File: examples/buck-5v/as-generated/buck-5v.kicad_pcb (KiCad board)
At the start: 2 copper layers, 126 x 56 mm, 11 parts, among them J1 12V IN, J2 5V OUT, U1 LM2596S-5

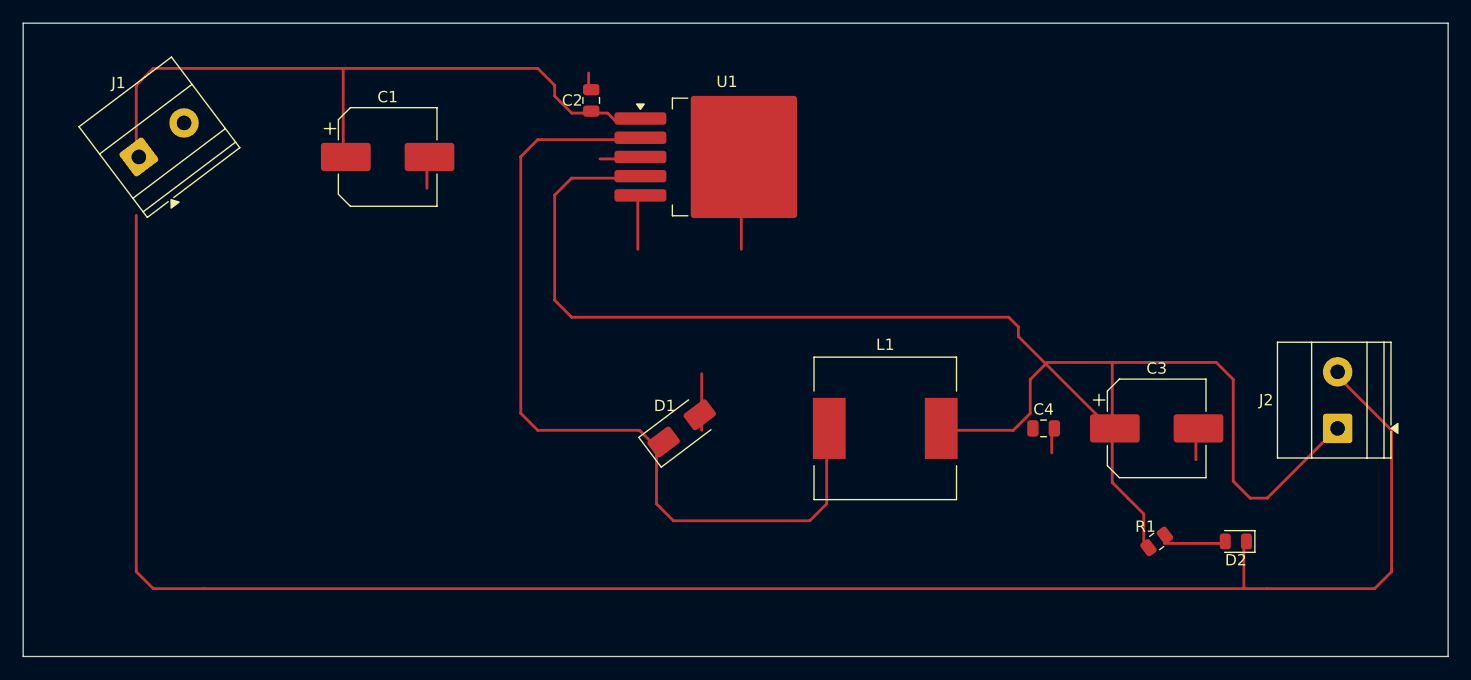
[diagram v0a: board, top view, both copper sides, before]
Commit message: Measure the copper that goes out and comes back, and the text drawn on text
The reviewer sent screenshots with circles on them. Two kinds: strings
printed through each other on the schematics, and copper that leaves a
pad, travels three sides of a rectangle and arrives four millimetres
away. Neither had a rule that could see it - `text_over_wire` measured
text against nets and nothing measured text against text, and
`route.detour` weighs a whole net, which averages one bad connection
away under any ratio worth setting.

New rule `route.wander`: one continuous run of copper - pad or junction
at each end - against the shortest way between those two ends that
clears the packages in between. The baseline walks the perimeter of
whatever the straight line crosses, so an opamp's feedback wrap is
measured against going round the package rather than through it. On
KiCad's 18 demo boards it fires once at the shipped 2.0x.

`readability.text_over_text` and `_over_wire` are regraded info: they
fire on 14 and 10 of those 18 human sheets. That is the estimate
talking, not the drawing. `ai-generated` still promotes both to errors,
so every generated design has to have none - and the five examples do.

What the two rules then made us fix:

* a net label's anchor cannot move, but its reading direction can. Each
  name is now offered the four quarters of its anchor and takes the
  first that prints over nothing. Power symbol names and PWR_FLAG names
  get the same treatment - four grounds on one row printed GNGNGNGND.
  Schematic text overlaps: buck 1, motor 2, carrier 1, fpga 7, all to 0.
* a plane crossing was priced at forty times front copper per
  millimetre, which is a prohibition, not a price: one millimetre of
  crossing bought a forty millimetre tour and the boards had grown
  them. Thirty is where neither `route.wander` nor `route.return_path`
  fires. Buck, motor and carrier now have no wander findings.
* `write_variant` resolves the routes a second time, so the
  straight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
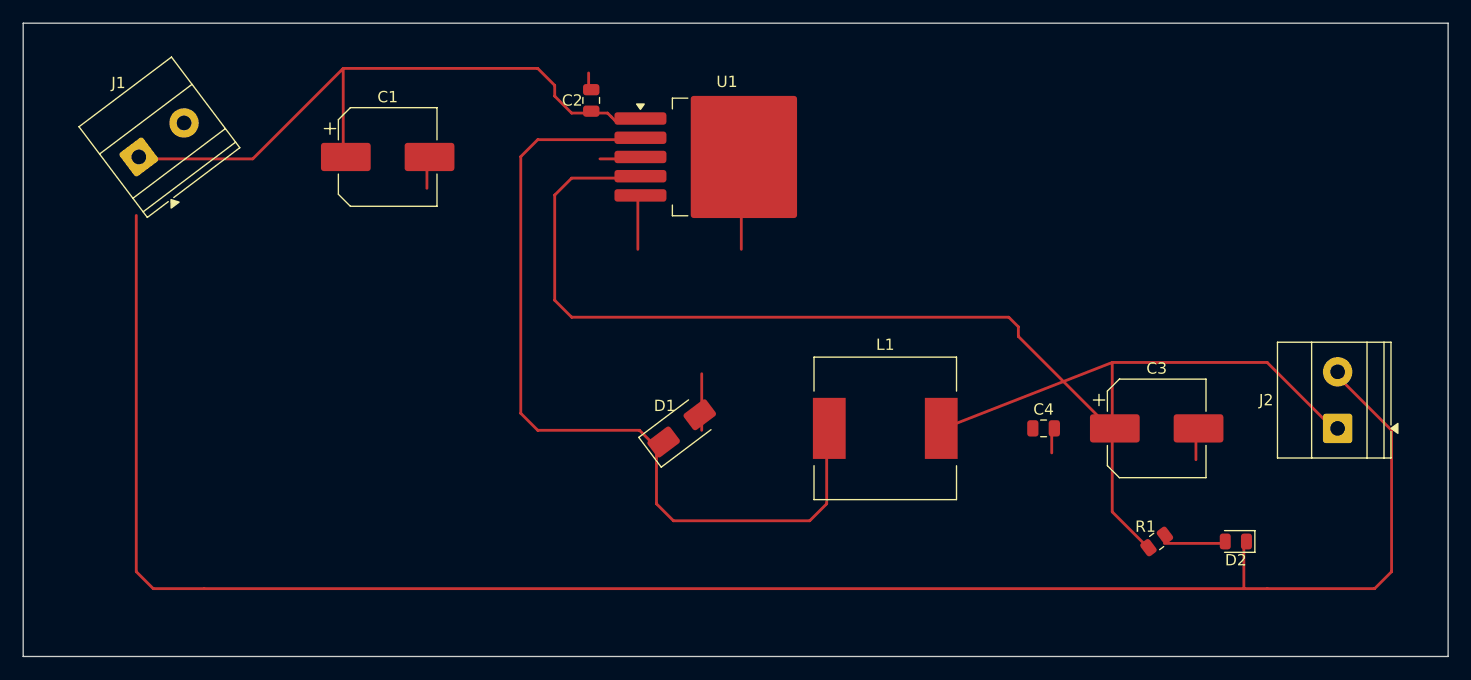
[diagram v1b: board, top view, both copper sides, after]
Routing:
- net /+5V: track 141.0 -> 127.7 mm
- net /+12V: track 61.9 -> 58.1 mm
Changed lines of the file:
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@@
 	(gr_line (start 226.0 116.0) (end 100.0 116.0) (stroke (width 0.1) (type default)) (layer "Edge.Cuts"))
 	(gr_line (start 100.0 116.0) (end 100.0 60.0) (stroke (width 0.1) (type default)) (layer "Edge.Cuts"))
-	(segment (start 110.0 72.0) (end 110.0 65.5) (width 0.25) (layer "F.Cu") (net 2))
-	(segment (start 110.0 65.5) (end 111.5 64.0) (width 0.25) (layer "F.Cu") (net 2))
-	(segment (start 111.5 64.0) (end 128.3 64.0) (width 0.25) (layer "F.Cu") (net 2))
+	(segment (start 110.0 72.0) (end 120.3 72.0) (width 0.25) (layer "F.Cu") (net 2))
+	(segment (start 120.3 72.0) (end 128.3 64.0) (width 0.25) (layer "F.Cu") (net 2))
 	(segment (start 128.3 64.0) (end 128.3 72.0) (width 0.25) (layer "F.Cu") (net 2))
 	(segment (start 128.3 64.0) (end 145.5 64.0) (width 0.25) (layer "F.Cu") (net 2))
@@
 	(segment (start 188.0 86.85) (end 188.0 87.7) (width 0.25) (layer "F.Cu") (net 3))
 	(segment (start 188.0 87.7) (end 196.3 96.0) (width 0.25) (layer "F.Cu") (net 3))
-	(segment (start 180.95 96.0) (end 187.55 96.0) (width 0.25) (layer "F.Cu") (net 3))
-	(segment (start 187.55 96.0) (end 189.05 94.5) (width 0.25) (layer "F.Cu") (net 3))
-	(segment (start 189.05 94.5) (end 189.05 91.5) (width 0.25) (layer "F.Cu") (net 3))
-	(segment (start 189.05 91.5) (end 190.55 90.0) (width 0.25) (layer "F.Cu") (net 3))
-	(segment (start 190.55 90.0) (end 196.3 90.0) (width 0.25) (layer "F.Cu") (net 3))
+	(segment (start 180.95 96.0) (end 196.3 90.0) (width 0.25) (layer "F.Cu") (net 3))
 	(segment (start 196.3 90.0) (end 196.3 96.0) (width 0.25) (layer "F.Cu") (net 3))
-	(segment (start 196.3 90.0) (end 205.5 90.0) (width 0.25) (layer "F.Cu") (net 3))
-	(segment (start 205.5 90.0) (end 207.0 91.5) (width 0.25) (layer "F.Cu") (net 3))
-	(segment (start 207.0 91.5) (end 207.0 100.5) (width 0.25) (layer "F.Cu") (net 3))
-	(segment (start 207.0 100.5) (end 208.5 102.0) (width 0.25) (layer "F.Cu") (net 3))
-	(segment (start 208.5 102.0) (end 210.0 102.0) (width 0.25) (layer "F.Cu") (net 3))
-	(segment (start 210.0 102.0) (end 216.0 96.0) (width 0.25) (layer "F.Cu") (net 3))
-	(segment (start 196.3 96.0) (end 196.3 100.606) (width 0.25) (layer "F.Cu") (net 3))
-	(segment (start 196.3 100.606) (end 197.694 102.0) (width 0.25) (layer "F.Cu") (net 3))
-	(segment (start 197.694 102.0) (end 199.088 103.394) (width 0.25) (layer "F.Cu") (net 3))
-	(segment (start 199.088 103.394) (end 199.0875 106.0) (width 0.25) (layer "F.Cu") (net 3))
+	(segment (start 196.3 90.0) (end 210.0 90.0) (width 0.25) (layer "F.Cu") (net 3))
+	(segment (start 210.0 90.0) (end 216.0 96.0) (width 0.25) (layer "F.Cu") (net 3))
+	(segment (start 196.3 96.0) (end 196.3 103.2125) (width 0.25) (layer "F.Cu") (net 3))
+	(segment (start 196.3 103.2125) (end 199.0875 106.0) (width 0.25) (layer "F.Cu") (net 3))
 	(segment (start 200.9125 106.0) (end 206.0625 106.0) (width 0.25) (layer "F.Cu") (net 4))
 	(segment (start 110.0 77.0) (end 110.0 108.5) (width 0.25) (layer "F.Cu") (net 1))

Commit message: Stop hiding the hairpins behind the pads they are drawn on
The reviewer said the 135 degree bends and the odd-angle runs were still
there. They were. `route.acute_angle` skipped any corner within a pad's
*radius*, and a 0805's radius is 0.47 mm, which covers the five or six
ordinary corners a chamfered pad entry leaves inside it. Eleven of the
thirteen hairpins on these five boards sat in that shadow, because a pad
is exactly where a route that has to double back does it.

The exemption is the pad's connection point now, not a disc around it.
Two branches leaving one pad stay exempt - the pad's own copper fills the
wedge, so it is not an acid trap - but nought degrees never is: that is
one run drawn twice, and no pad excuses it.

Then the generator had to stop making them:

* `_untraced` drops the copper a second run lays on top of the first.
  The shorter is inside the longer and carries nothing it does not; both
  get trimmed, because dropping only the duplicate leaves the other
  hanging over the gap, which is `route.stub`. It runs before the runs
  are joined, while the pair is still two tracks sharing an end - once
  joined, the shared point is usually a pad, and the clean-up passes pin
  those precisely so they cannot take copper off them.
* `_straighten` only takes the direct line when it lands on the 45 grid.
  Between two pads at whatever coordinates their packages give them it
  usually does not: last round it made a nine millimetre run at 169.7
  degrees, which is the slip-of-the-mouse angle `route.odd_angle` is for.

Measured across the five boards: off-grid segments 1 to 0, 180 degree
reversals 6 to 0, and the motor board's `route.return_path` finding went
with the 11 mm of copper it was measuring.

Three corners survive, all on the FPGA board, all where a knee lands a
fraction past where its own two legs cross - legs of 0.07 and 0.25 mm on
two, 0.15 and 0.5 mm on the third. Refusing a knee that short is worse:
the segment then keeps the angle it had, a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
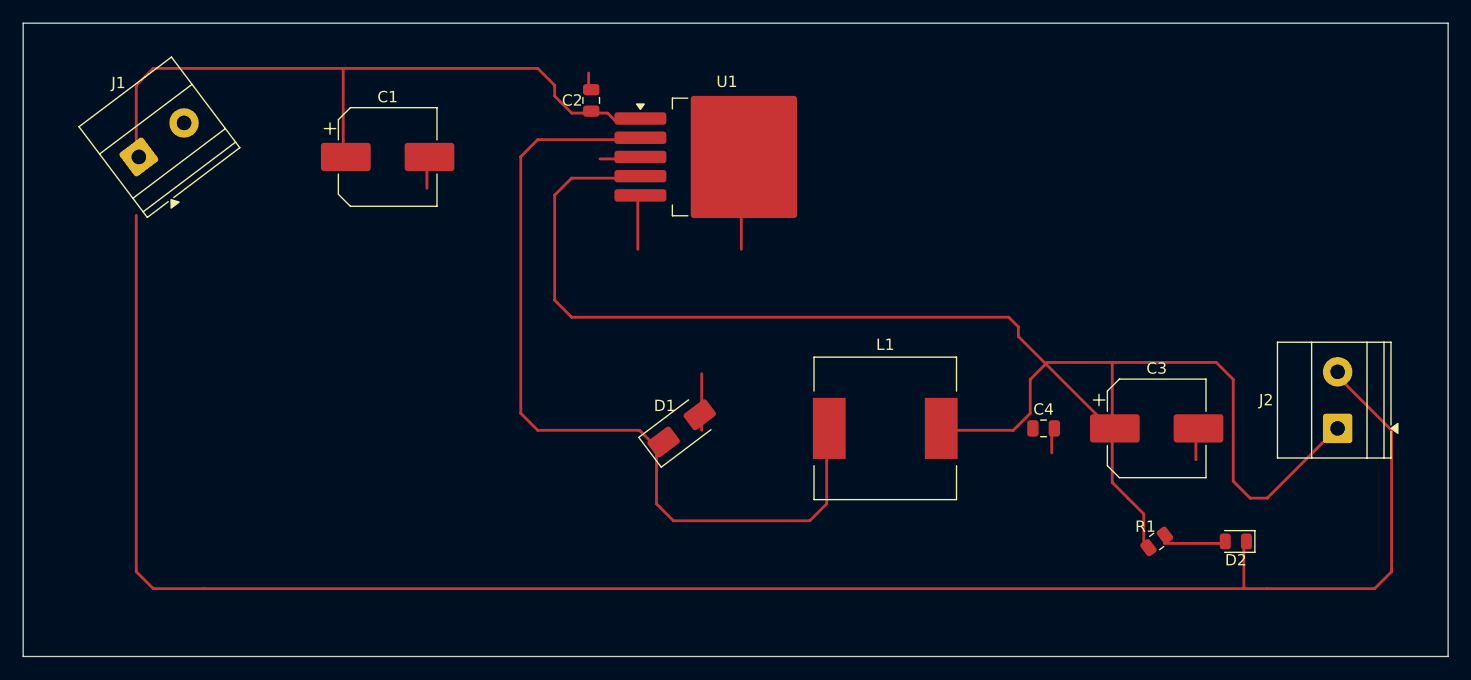
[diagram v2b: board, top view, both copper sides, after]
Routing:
- net /+5V: track 127.7 -> 141.0 mm
- net /+12V: track 58.1 -> 61.9 mm
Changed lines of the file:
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@@
 	(gr_line (start 226.0 116.0) (end 100.0 116.0) (stroke (width 0.1) (type default)) (layer "Edge.Cuts"))
 	(gr_line (start 100.0 116.0) (end 100.0 60.0) (stroke (width 0.1) (type default)) (layer "Edge.Cuts"))
-	(segment (start 110.0 72.0) (end 120.3 72.0) (width 0.25) (layer "F.Cu") (net 2))
-	(segment (start 120.3 72.0) (end 128.3 64.0) (width 0.25) (layer "F.Cu") (net 2))
+	(segment (start 110.0 72.0) (end 110.0 65.5) (width 0.25) (layer "F.Cu") (net 2))
+	(segment (start 110.0 65.5) (end 111.5 64.0) (width 0.25) (layer "F.Cu") (net 2))
+	(segment (start 111.5 64.0) (end 128.3 64.0) (width 0.25) (layer "F.Cu") (net 2))
 	(segment (start 128.3 64.0) (end 128.3 72.0) (width 0.25) (layer "F.Cu") (net 2))
 	(segment (start 128.3 64.0) (end 145.5 64.0) (width 0.25) (layer "F.Cu") (net 2))
@@
 	(segment (start 188.0 86.85) (end 188.0 87.7) (width 0.25) (layer "F.Cu") (net 3))
 	(segment (start 188.0 87.7) (end 196.3 96.0) (width 0.25) (layer "F.Cu") (net 3))
-	(segment (start 180.95 96.0) (end 196.3 90.0) (width 0.25) (layer "F.Cu") (net 3))
+	(segment (start 180.95 96.0) (end 187.55 96.0) (width 0.25) (layer "F.Cu") (net 3))
+	(segment (start 187.55 96.0) (end 189.05 94.5) (width 0.25) (layer "F.Cu") (net 3))
+	(segment (start 189.05 94.5) (end 189.05 91.5) (width 0.25) (layer "F.Cu") (net 3))
+	(segment (start 189.05 91.5) (end 190.55 90.0) (width 0.25) (layer "F.Cu") (net 3))
+	(segment (start 190.55 90.0) (end 196.3 90.0) (width 0.25) (layer "F.Cu") (net 3))
 	(segment (start 196.3 90.0) (end 196.3 96.0) (width 0.25) (layer "F.Cu") (net 3))
-	(segment (start 196.3 90.0) (end 210.0 90.0) (width 0.25) (layer "F.Cu") (net 3))
-	(segment (start 210.0 90.0) (end 216.0 96.0) (width 0.25) (layer "F.Cu") (net 3))
-	(segment (start 196.3 96.0) (end 196.3 103.2125) (width 0.25) (layer "F.Cu") (net 3))
-	(segment (start 196.3 103.2125) (end 199.0875 106.0) (width 0.25) (layer "F.Cu") (net 3))
+	(segment (start 196.3 90.0) (end 205.5 90.0) (width 0.25) (layer "F.Cu") (net 3))
+	(segment (start 205.5 90.0) (end 207.0 91.5) (width 0.25) (layer "F.Cu") (net 3))
+	(segment (start 207.0 91.5) (end 207.0 100.5) (width 0.25) (layer "F.Cu") (net 3))
+	(segment (start 207.0 100.5) (end 208.5 102.0) (width 0.25) (layer "F.Cu") (net 3))
+	(segment (start 208.5 102.0) (end 210.0 102.0) (width 0.25) (layer "F.Cu") (net 3))
+	(segment (start 210.0 102.0) (end 216.0 96.0) (width 0.25) (layer "F.Cu") (net 3))
+	(segment (start 196.3 96.0) (end 196.3 100.606) (width 0.25) (layer "F.Cu") (net 3))
+	(segment (start 196.3 100.606) (end 197.694 102.0) (width 0.25) (layer "F.Cu") (net 3))
+	(segment (start 197.694 102.0) (end 199.088 103.394) (width 0.25) (layer "F.Cu") (net 3))
+	(segment (start 199.088 103.394) (end 199.0875 106.0) (width 0.25) (layer "F.Cu") (net 3))
 	(segment (start 200.9125 106.0) (end 206.0625 106.0) (width 0.25) (layer "F.Cu") (net 4))
 	(segment (start 110.0 77.0) (end 110.0 108.5) (width 0.25) (layer "F.Cu") (net 1))
